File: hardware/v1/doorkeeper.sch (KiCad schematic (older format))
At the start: 29 parts, among them K1 RELAYPTH, K2 relay output, P1 ESP01 PROGRAMMING PORT, P2 ESP-01, P3 Vin, P4 ARDU PROGRAMMING PORT, P5 Software serial, P6 OLED I2C, P7 RC522, P8 Spare Pins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

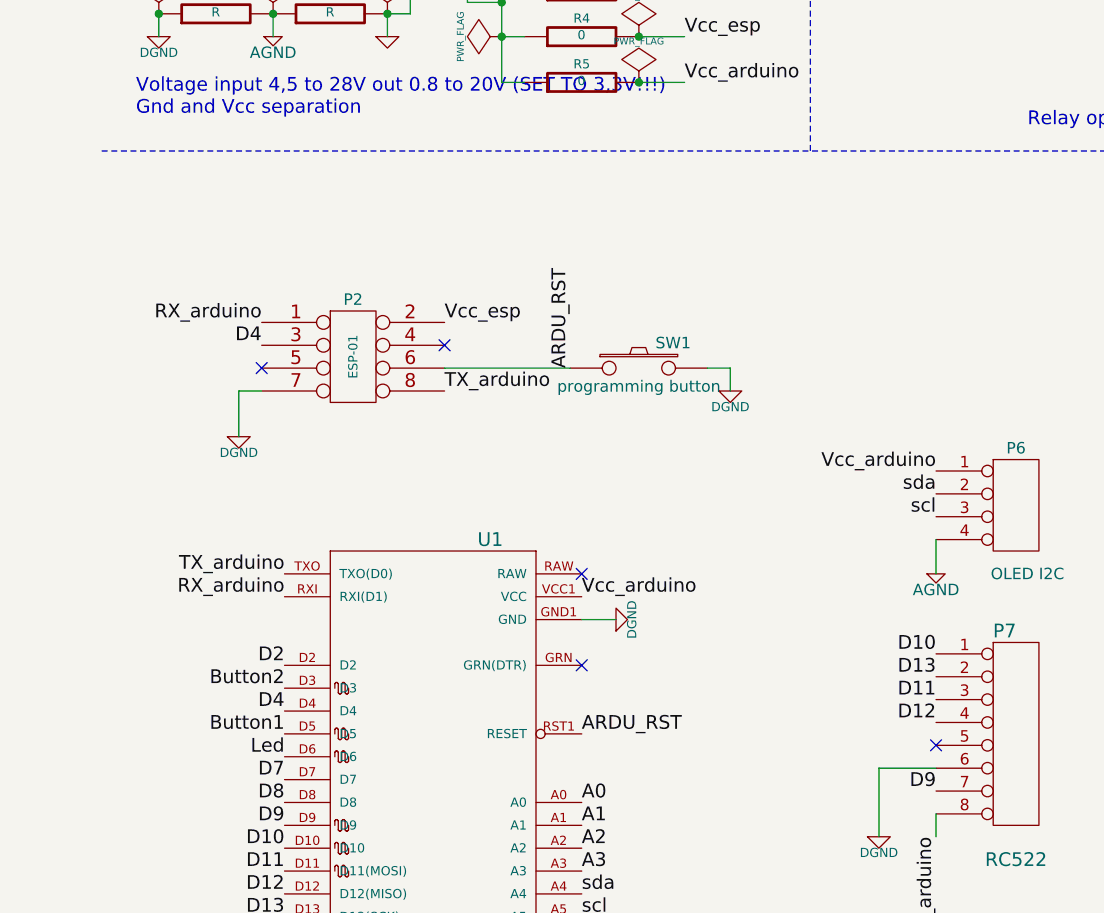
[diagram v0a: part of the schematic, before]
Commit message: corrected a schematic
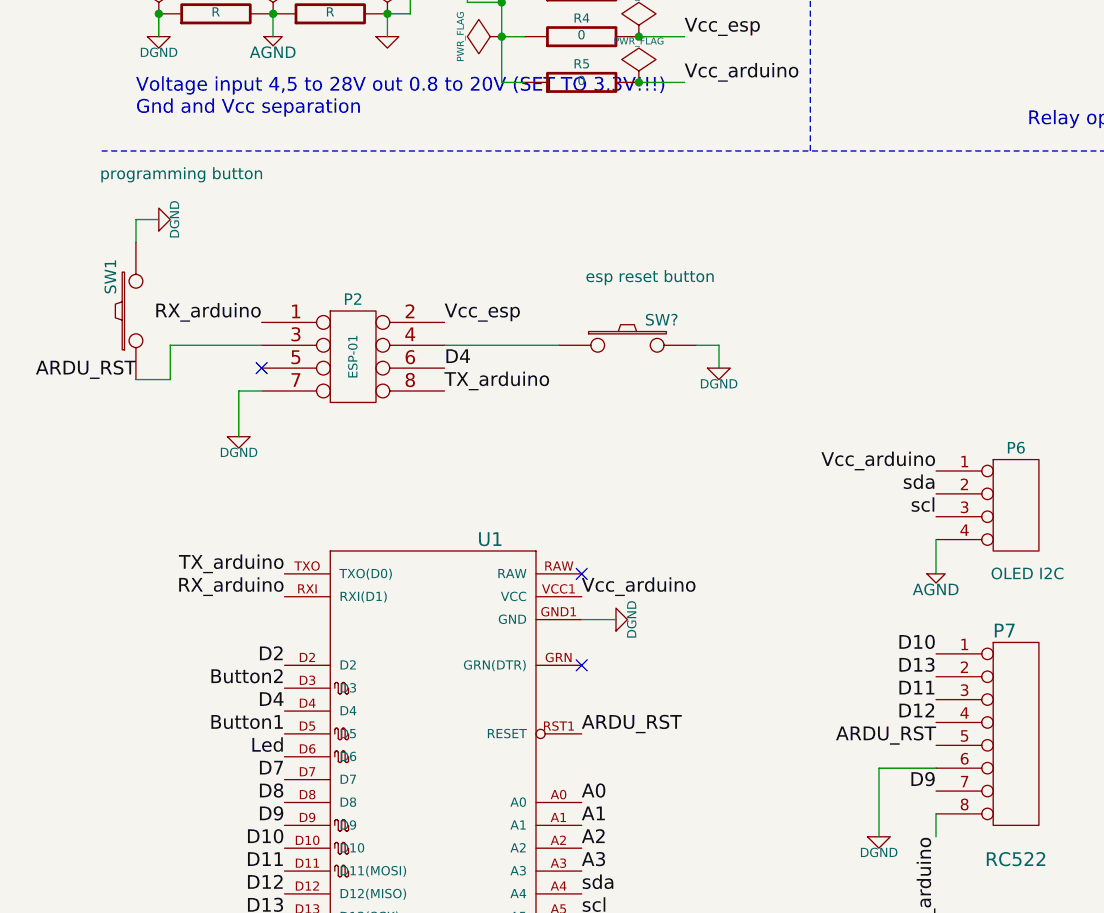
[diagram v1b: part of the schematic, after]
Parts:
- added SW?: esp reset button, ~, symbol SW_PUSH
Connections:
- net ARDU_RST: now also P2.3 (CH_PD), P7.5 (P5); no longer P2.6 (GPIO0)
- net D4: now also P2.6 (GPIO0); no longer P2.3 (CH_PD)
- net DGND: now also SW?.2
- net at P2.4 (GPIO2): now also SW?.1
- no-connect marks 6 -> 4
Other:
- moved on the sheet: SW1
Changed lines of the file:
@@
 Sheet 1 1
 Title ""
-Date "5 may 2015"
+Date "6 may 2015"
 Rev ""
 Comp ""
@@
 Text Label 1200 3650 2    60   ~ 0
 RX_arduino
-Text Label 1200 3750 2    60   ~ 0
-D4
 Text Label 1300 5350 2    60   ~ 0
 D4
@@
 Wire Wire Line
 	1100 3950 1100 4150
-NoConn ~ 2000 3750
 NoConn ~ 1200 3850
 $Comp
@@
 L SW_PUSH SW1
 U 1 1 554907CD
-P 2850 3850
-F 0 "SW1" H 3000 3960 50  0000 C CNN
-F 1 "programming button" H 2850 3770 50  0000 C CNN
-F 2 "~" H 2850 3850 60  0000 C CNN
-F 3 "~" H 2850 3850 60  0000 C CNN
-	1    2850 3850
-	1    0    0    -1
-$EndComp
-Wire Wire Line
-	3150 3850 3250 3850
-Wire Wire Line
-	3250 3850 3250 3950
+P 650 3600
+F 0 "SW1" H 800 3710 50  0000 C CNN
+F 1 "programming button" V 1250 3400 50  0000 C CNN
+F 2 "~" H 650 3600 60  0000 C CNN
+F 3 "~" H 650 3600 60  0000 C CNN
+	1    650  3600
+	0    -1   -1   0
+$EndComp
+Wire Wire Line
+	650  3300 650  3200
+Wire Wire Line
+	650  3200 750  3200
 $Comp
 L DGND #PWR012
 U 1 1 55490841
-P 3250 3950
-F 0 "#PWR012" H 3250 3950 40  0001 C CNN
-F 1 "DGND" H 3250 3880 40  0000 C CNN
-F 2 "~" H 3250 3950 60  0000 C CNN
-F 3 "~" H 3250 3950 60  0000 C CNN
-	1    3250 3950
-	1    0    0    -1
+P 750 3200
+F 0 "#PWR012" H 750 3200 40  0001 C CNN
+F 1 "DGND" H 750 3130 40  0000 C CNN
+F 2 "~" H 750 3200 60  0000 C CNN
+F 3 "~" H 750 3200 60  0000 C CNN
+	1    750  3200
+	0    -1   -1   0
 $EndComp
 $Comp
@@
 	1    0    0    -1
 $EndComp
-NoConn ~ 4150 5500
 Wire Wire Line
 	4150 5600 3900 5600
@@
 Text Label 4150 5400 2    60   ~ 0
 D12
-Wire Wire Line
-	2000 3850 2550 3850
-Text Label 2550 3850 1    60   ~ 0
+Text Label 650  3900 2    60   ~ 0
 ARDU_RST
 $Comp
@@
 Wire Wire Line
 	2850 2600 3050 2600
+Text Label 4150 5500 2    60   ~ 0
+ARDU_RST
+Wire Wire Line
+	650  3900 800  3900
+Wire Wire Line
+	800  3900 800  3750
+Wire Wire Line
+	800  3750 1200 3750
+Wire Wire Line
+	2000 3750 2500 3750
+$Comp
+L SW_PUSH SW?
+U 1 1 554A5A58
+P 2800 3750
+F 0 "SW?" H 2950 3860 50  0000 C CNN
+F 1 "esp reset button" H 2900 4050 50  0000 C CNN
+F 2 "~" H 2800 3750 60  0000 C CNN
+F 3 "~" H 2800 3750 60  0000 C CNN
+	1    2800 3750
+	1    0    0    -1
+$EndComp
+Wire Wire Line
+	3100 3750 3200 3750
+Wire Wire Line
+	3200 3750 3200 3850
+$Comp
+L DGND #PWR?
+U 1 1 554A5A60
+P 3200 3850
+F 0 "#PWR?" H 3200 3850 40  0001 C CNN
+F 1 "DGND" H 3200 3780 40  0000 C CNN
+F 2 "~" H 3200 3850 60  0000 C CNN
+F 3 "~" H 3200 3850 60  0000 C CNN
+	1    3200 3850
+	1    0    0    -1
+$EndComp
+Text Label 2000 3850 0    60   ~ 0
+D4
 $EndSCHEMATC

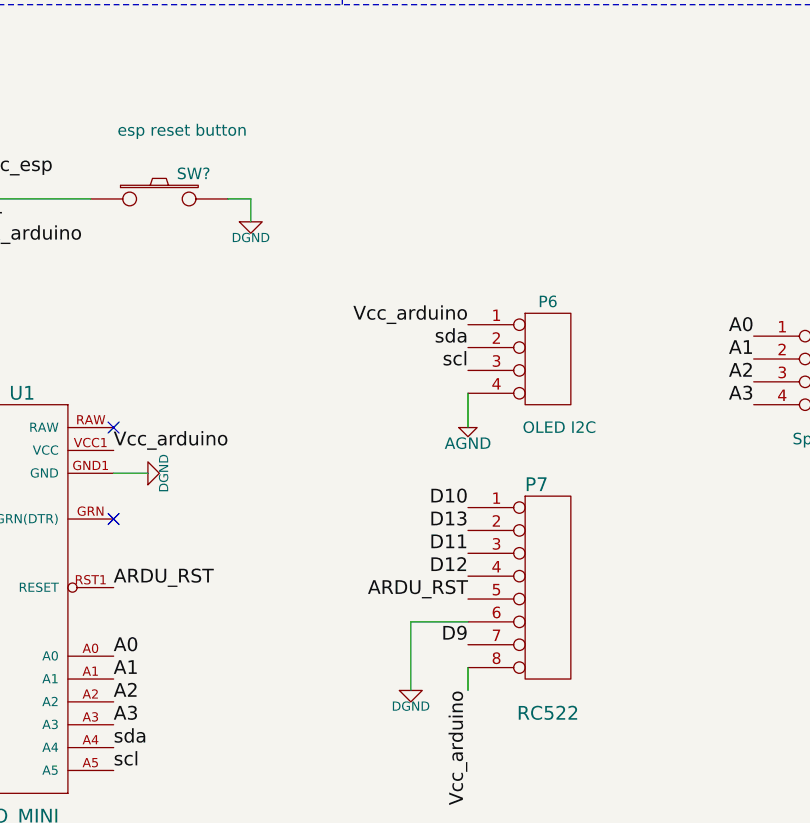
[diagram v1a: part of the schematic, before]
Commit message: corrected a schematic
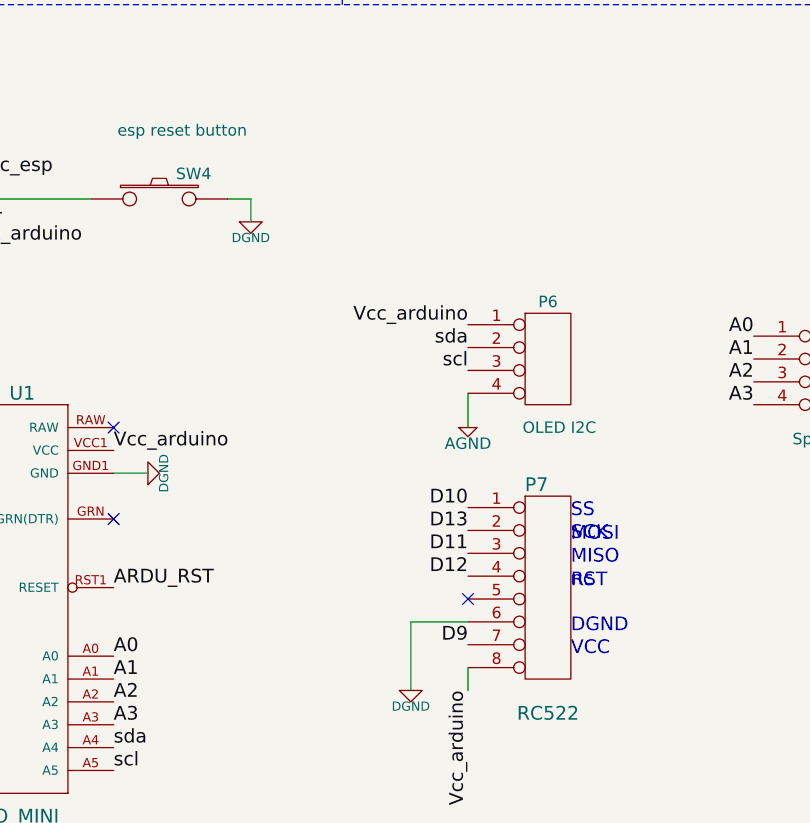
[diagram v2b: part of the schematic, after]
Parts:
- gave numbers to parts that had none: 1
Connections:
- net ARDU_RST: no longer P7.5 (P5)
- no-connect marks 4 -> 5
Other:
- note added: "DGND\n\n"
- note added: "MISO\n\n"
- note added: "MOSI\n\n"
- note added: "RST\n\n\n"
- note added: "SCK\n"
- note added: "SS"
- note added: "VCC\n\n"
- note added: "nc\n\n"
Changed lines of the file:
@@
 	750  2300 750  2400
 $Comp
-L DGND #PWR01
+L DGND #PWR1
 U 1 1 554902C3
 P 750 2400
-F 0 "#PWR01" H 750 2400 40  0001 C CNN
+F 0 "#PWR1" H 750 2400 40  0001 C CNN
 F 1 "DGND" H 750 2330 40  0000 C CNN
 F 2 "~" H 750 2400 60  0000 C CNN
@@
 $EndComp
 $Comp
-L AGND #PWR02
+L AGND #PWR5
 U 1 1 554902D2
 P 1250 2400
-F 0 "#PWR02" H 1250 2400 40  0001 C CNN
+F 0 "#PWR5" H 1250 2400 40  0001 C CNN
 F 1 "AGND" H 1250 2330 50  0000 C CNN
 F 2 "~" H 1250 2400 60  0000 C CNN
@@
 $EndComp
 $Comp
-L GND #PWR03
+L GND #PWR6
 U 1 1 554902E1
 P 1750 2400
-F 0 "#PWR03" H 1750 2400 30  0001 C CNN
+F 0 "#PWR6" H 1750 2400 30  0001 C CNN
 F 1 "GND" H 1750 2330 30  0001 C CNN
 F 2 "~" H 1750 2400 60  0000 C CNN
@@
 $EndComp
 $Comp
-L PWR_FLAG #FLG04
+L PWR_FLAG #FLG1
 U 1 1 554902FF
 P 750 2300
-F 0 "#FLG04" H 750 2395 30  0001 C CNN
+F 0 "#FLG1" H 750 2395 30  0001 C CNN
 F 1 "PWR_FLAG" H 750 2480 30  0000 C CNN
 F 2 "~" H 750 2300 60  0000 C CNN
@@
 $EndComp
 $Comp
-L PWR_FLAG #FLG05
+L PWR_FLAG #FLG2
 U 1 1 5549030C
 P 1250 2300
-F 0 "#FLG05" H 1250 2395 30  0001 C CNN
+F 0 "#FLG2" H 1250 2395 30  0001 C CNN
 F 1 "PWR_FLAG" H 1250 2480 30  0000 C CNN
 F 2 "~" H 1250 2300 60  0000 C CNN
@@
 $EndComp
 $Comp
-L PWR_FLAG #FLG06
+L PWR_FLAG #FLG3
 U 1 1 55490312
 P 1750 2300
-F 0 "#FLG06" H 1750 2395 30  0001 C CNN
+F 0 "#FLG3" H 1750 2395 30  0001 C CNN
 F 1 "PWR_FLAG" H 1750 2480 30  0000 C CNN
 F 2 "~" H 1750 2300 60  0000 C CNN
@@
 Connection ~ 2250 2250
 $Comp
-L PWR_FLAG #FLG07
+L PWR_FLAG #FLG5
 U 1 1 55490369
 P 2850 2200
-F 0 "#FLG07" H 2850 2295 30  0001 C CNN
+F 0 "#FLG5" H 2850 2295 30  0001 C CNN
 F 1 "PWR_FLAG" H 2850 2380 30  0000 C CNN
 F 2 "~" H 2850 2200 60  0000 C CNN
@@
 Connection ~ 2250 2400
 $Comp
-L PWR_FLAG #FLG08
+L PWR_FLAG #FLG6
 U 1 1 554903BB
 P 2850 2400
-F 0 "#FLG08" H 2850 2495 30  0001 C CNN
+F 0 "#FLG6" H 2850 2495 30  0001 C CNN
 F 1 "PWR_FLAG" H 2850 2580 30  0000 C CNN
 F 2 "~" H 2850 2400 60  0000 C CNN
@@
 $EndComp
 $Comp
-L PWR_FLAG #FLG09
+L PWR_FLAG #FLG7
 U 1 1 554903C1
 P 2850 2600
-F 0 "#FLG09" H 2850 2695 30  0001 C CNN
+F 0 "#FLG7" H 2850 2695 30  0001 C CNN
 F 1 "PWR_FLAG" H 2850 2780 30  0000 C CNN
 F 2 "~" H 2850 2600 60  0000 C CNN
@@
 Connection ~ 2850 2600
 $Comp
-L GND #PWR010
+L GND #PWR14
 U 1 1 554904FE
 P 4950 2350
-F 0 "#PWR010" H 4950 2350 30  0001 C CNN
+F 0 "#PWR14" H 4950 2350 30  0001 C CNN
 F 1 "GND" H 4950 2280 30  0001 C CNN
 F 2 "~" H 4950 2350 60  0000 C CNN
@@
 Vcc_relay
 $Comp
-L DGND #PWR011
+L DGND #PWR3
 U 1 1 5549054D
 P 1100 4150
-F 0 "#PWR011" H 1100 4150 40  0001 C CNN
+F 0 "#PWR3" H 1100 4150 40  0001 C CNN
 F 1 "DGND" H 1100 4080 40  0000 C CNN
 F 2 "~" H 1100 4150 60  0000 C CNN
@@
 	650  3200 750  3200
 $Comp
-L DGND #PWR012
+L DGND #PWR2
 U 1 1 55490841
 P 750 3200
-F 0 "#PWR012" H 750 3200 40  0001 C CNN
+F 0 "#PWR2" H 750 3200 40  0001 C CNN
 F 1 "DGND" H 750 3130 40  0000 C CNN
 F 2 "~" H 750 3200 60  0000 C CNN
@@
 $EndComp
 $Comp
-L DGND #PWR013
+L DGND #PWR4
 U 1 1 5549087F
 P 1100 7150
-F 0 "#PWR013" H 1100 7150 40  0001 C CNN
+F 0 "#PWR4" H 1100 7150 40  0001 C CNN
 F 1 "DGND" H 1100 7080 40  0000 C CNN
 F 2 "~" H 1100 7150 60  0000 C CNN
@@
 RX_arduino
 $Comp
-L DGND #PWR014
+L DGND #PWR7
 U 1 1 554908C1
 P 2200 7150
-F 0 "#PWR014" H 2200 7150 40  0001 C CNN
+F 0 "#PWR7" H 2200 7150 40  0001 C CNN
 F 1 "DGND" H 2200 7080 40  0000 C CNN
 F 2 "~" H 2200 7150 60  0000 C CNN
@@
 	4150 5800 4150 5900
 $Comp
-L DGND #PWR015
+L DGND #PWR12
 U 1 1 55490C81
 P 3900 5900
-F 0 "#PWR015" H 3900 5900 40  0001 C CNN
+F 0 "#PWR12" H 3900 5900 40  0001 C CNN
 F 1 "DGND" H 3900 5830 40  0000 C CNN
 F 2 "~" H 3900 5900 60  0000 C CNN
@@
 scl
 $Comp
-L AGND #PWR016
+L AGND #PWR13
 U 1 1 55490FC0
 P 4150 4750
-F 0 "#PWR016" H 4150 4750 40  0001 C CNN
+F 0 "#PWR13" H 4150 4750 40  0001 C CNN
 F 1 "AGND" H 4150 4680 50  0000 C CNN
 F 2 "~" H 4150 4750 60  0000 C CNN
@@
 NoConn ~ 2600 4750
 $Comp
-L DGND #PWR017
+L DGND #PWR8
 U 1 1 55491065
 P 2750 4950
-F 0 "#PWR017" H 2750 4950 40  0001 C CNN
+F 0 "#PWR8" H 2750 4950 40  0001 C CNN
 F 1 "DGND" H 2750 4880 40  0000 C CNN
 F 2 "~" H 2750 4950 60  0000 C CNN
@@
 	8300 2050 8300 2300
 $Comp
-L GND #PWR018
+L GND #PWR15
 U 1 1 554911B9
 P 8300 2300
-F 0 "#PWR018" H 8300 2300 30  0001 C CNN
+F 0 "#PWR15" H 8300 2300 30  0001 C CNN
 F 1 "GND" H 8300 2230 30  0001 C CNN
 F 2 "~" H 8300 2300 60  0000 C CNN
@@
 	3850 6700 3850 6750
 $Comp
-L DGND #PWR019
+L DGND #PWR10
 U 1 1 554913C9
 P 3850 6750
-F 0 "#PWR019" H 3850 6750 40  0001 C CNN
+F 0 "#PWR10" H 3850 6750 40  0001 C CNN
 F 1 "DGND" H 3850 6680 40  0000 C CNN
 F 2 "~" H 3850 6750 60  0000 C CNN
@@
 	3850 7100 3850 7150
 $Comp
-L DGND #PWR020
+L DGND #PWR11
 U 1 1 554913E5
 P 3850 7150
-F 0 "#PWR020" H 3850 7150 40  0001 C CNN
+F 0 "#PWR11" H 3850 7150 40  0001 C CNN
 F 1 "DGND" H 3850 7080 40  0000 C CNN
 F 2 "~" H 3850 7150 60  0000 C CNN
@@
 A3
 $Comp
-L PWR_FLAG #FLG021
+L PWR_FLAG #FLG4
 U 1 1 55491BE4
 P 2250 2400
-F 0 "#FLG021" H 2250 2495 30  0001 C CNN
+F 0 "#FLG4" H 2250 2495 30  0001 C CNN
 F 1 "PWR_FLAG" H 2250 2580 30  0000 C CNN
 F 2 "~" H 2250 2400 60  0000 C CNN
@@
 Wire Wire Line
 	2850 2600 3050 2600
-Text Label 4150 5500 2    60   ~ 0
-ARDU_RST
 Wire Wire Line
 	650  3900 800  3900
@@
 	2000 3750 2500 3750
 $Comp
-L SW_PUSH SW?
+L SW_PUSH SW4
 U 1 1 554A5A58
 P 2800 3750
-F 0 "SW?" H 2950 3860 50  0000 C CNN
+F 0 "SW4" H 2950 3860 50  0000 C CNN
 F 1 "esp reset button" H 2900 4050 50  0000 C CNN
 F 2 "~" H 2800 3750 60  0000 C CNN
@@
 	3200 3750 3200 3850
 $Comp
-L DGND #PWR?
+L DGND #PWR9
 U 1 1 554A5A60
 P 3200 3850
-F 0 "#PWR?" H 3200 3850 40  0001 C CNN
+F 0 "#PWR9" H 3200 3850 40  0001 C CNN
 F 1 "DGND" H 3200 3780 40  0000 C CNN
 F 2 "~" H 3200 3850 60  0000 C CNN
@@
 Text Label 2000 3850 0    60   ~ 0
 D4
+Text Notes 4600 5150 0    60   ~ 0
+SS
+Text Notes 4600 5250 0    60   ~ 0
+SCK\n
+NoConn ~ 4150 5500
+Text Notes 4600 5350 0    60   ~ 0
+MOSI\n\n
+Text Notes 4600 5450 0    60   ~ 0
+MISO\n\n
+Text Notes 4600 5550 0    60   ~ 0
+nc\n\n
+Text Notes 4600 5650 0    60   ~ 0
+RST\n\n\n
+Text Notes 4600 5850 0    60   ~ 0
+VCC\n\n
+Text Notes 4600 5750 0    60   ~ 0
+DGND\n\n
 $EndSCHEMATC

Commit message: partial routing
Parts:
- R1, R2: value R -> 0
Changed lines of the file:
@@
 Sheet 1 1
 Title ""
-Date "6 may 2015"
+Date "8 may 2015"
 Rev ""
 Comp ""
@@
 	750  2300 750  2400
 $Comp
-L DGND #PWR1
+L DGND #PWR01
 U 1 1 554902C3
 P 750 2400
-F 0 "#PWR1" H 750 2400 40  0001 C CNN
+F 0 "#PWR01" H 750 2400 40  0001 C CNN
 F 1 "DGND" H 750 2330 40  0000 C CNN
 F 2 "~" H 750 2400 60  0000 C CNN
@@
 $EndComp
 $Comp
-L AGND #PWR5
+L AGND #PWR02
 U 1 1 554902D2
 P 1250 2400
-F 0 "#PWR5" H 1250 2400 40  0001 C CNN
+F 0 "#PWR02" H 1250 2400 40  0001 C CNN
 F 1 "AGND" H 1250 2330 50  0000 C CNN
 F 2 "~" H 1250 2400 60  0000 C CNN
@@
 $EndComp
 $Comp
-L GND #PWR6
+L GND #PWR03
 U 1 1 554902E1
 P 1750 2400
-F 0 "#PWR6" H 1750 2400 30  0001 C CNN
+F 0 "#PWR03" H 1750 2400 30  0001 C CNN
 F 1 "GND" H 1750 2330 30  0001 C CNN
 F 2 "~" H 1750 2400 60  0000 C CNN
@@
 $EndComp
 $Comp
-L PWR_FLAG #FLG1
+L PWR_FLAG #FLG04
 U 1 1 554902FF
 P 750 2300
-F 0 "#FLG1" H 750 2395 30  0001 C CNN
+F 0 "#FLG04" H 750 2395 30  0001 C CNN
 F 1 "PWR_FLAG" H 750 2480 30  0000 C CNN
 F 2 "~" H 750 2300 60  0000 C CNN
@@
 $EndComp
 $Comp
-L PWR_FLAG #FLG2
+L PWR_FLAG #FLG05
 U 1 1 5549030C
 P 1250 2300
-F 0 "#FLG2" H 1250 2395 30  0001 C CNN
+F 0 "#FLG05" H 1250 2395 30  0001 C CNN
 F 1 "PWR_FLAG" H 1250 2480 30  0000 C CNN
 F 2 "~" H 1250 2300 60  0000 C CNN
@@
 $EndComp
 $Comp
-L PWR_FLAG #FLG3
+L PWR_FLAG #FLG06
 U 1 1 55490312
 P 1750 2300
-F 0 "#FLG3" H 1750 2395 30  0001 C CNN
+F 0 "#FLG06" H 1750 2395 30  0001 C CNN
 F 1 "PWR_FLAG" H 1750 2480 30  0000 C CNN
 F 2 "~" H 1750 2300 60  0000 C CNN
@@
 Connection ~ 2250 2250
 $Comp
-L PWR_FLAG #FLG5
+L PWR_FLAG #FLG07
 U 1 1 55490369
 P 2850 2200
-F 0 "#FLG5" H 2850 2295 30  0001 C CNN
+F 0 "#FLG07" H 2850 2295 30  0001 C CNN
 F 1 "PWR_FLAG" H 2850 2380 30  0000 C CNN
 F 2 "~" H 2850 2200 60  0000 C CNN
@@
 Connection ~ 2250 2400
 $Comp
-L PWR_FLAG #FLG6
+L PWR_FLAG #FLG08
 U 1 1 554903BB
 P 2850 2400
-F 0 "#FLG6" H 2850 2495 30  0001 C CNN
+F 0 "#FLG08" H 2850 2495 30  0001 C CNN
 F 1 "PWR_FLAG" H 2850 2580 30  0000 C CNN
 F 2 "~" H 2850 2400 60  0000 C CNN
@@
 $EndComp
 $Comp
-L PWR_FLAG #FLG7
+L PWR_FLAG #FLG09
 U 1 1 554903C1
 P 2850 2600
-F 0 "#FLG7" H 2850 2695 30  0001 C CNN
+F 0 "#FLG09" H 2850 2695 30  0001 C CNN
 F 1 "PWR_FLAG" H 2850 2780 30  0000 C CNN
 F 2 "~" H 2850 2600 60  0000 C CNN
@@
 Connection ~ 2850 2600
 $Comp
-L GND #PWR14
+L GND #PWR010
 U 1 1 554904FE
 P 4950 2350
-F 0 "#PWR14" H 4950 2350 30  0001 C CNN
+F 0 "#PWR010" H 4950 2350 30  0001 C CNN
 F 1 "GND" H 4950 2280 30  0001 C CNN
 F 2 "~" H 4950 2350 60  0000 C CNN
@@
 Vcc_relay
 $Comp
-L DGND #PWR3
+L DGND #PWR011
 U 1 1 5549054D
 P 1100 4150
-F 0 "#PWR3" H 1100 4150 40  0001 C CNN
+F 0 "#PWR011" H 1100 4150 40  0001 C CNN
 F 1 "DGND" H 1100 4080 40  0000 C CNN
 F 2 "~" H 1100 4150 60  0000 C CNN
@@
 	650  3200 750  3200
 $Comp
-L DGND #PWR2
+L DGND #PWR012
 U 1 1 55490841
 P 750 3200
-F 0 "#PWR2" H 750 3200 40  0001 C CNN
+F 0 "#PWR012" H 750 3200 40  0001 C CNN
 F 1 "DGND" H 750 3130 40  0000 C CNN
 F 2 "~" H 750 3200 60  0000 C CNN
@@
 $EndComp
 $Comp
-L DGND #PWR4
+L DGND #PWR013
 U 1 1 5549087F
 P 1100 7150
-F 0 "#PWR4" H 1100 7150 40  0001 C CNN
+F 0 "#PWR013" H 1100 7150 40  0001 C CNN
 F 1 "DGND" H 1100 7080 40  0000 C CNN
 F 2 "~" H 1100 7150 60  0000 C CNN
@@
 RX_arduino
 $Comp
-L DGND #PWR7
+L DGND #PWR014
 U 1 1 554908C1
 P 2200 7150
-F 0 "#PWR7" H 2200 7150 40  0001 C CNN
+F 0 "#PWR014" H 2200 7150 40  0001 C CNN
 F 1 "DGND" H 2200 7080 40  0000 C CNN
 F 2 "~" H 2200 7150 60  0000 C CNN
@@
 	4150 5800 4150 5900
 $Comp
-L DGND #PWR12
+L DGND #PWR015
 U 1 1 55490C81
 P 3900 5900
-F 0 "#PWR12" H 3900 5900 40  0001 C CNN
+F 0 "#PWR015" H 3900 5900 40  0001 C CNN
 F 1 "DGND" H 3900 5830 40  0000 C CNN
 F 2 "~" H 3900 5900 60  0000 C CNN
@@
 scl
 $Comp
-L AGND #PWR13
+L AGND #PWR016
 U 1 1 55490FC0
 P 4150 4750
-F 0 "#PWR13" H 4150 4750 40  0001 C CNN
+F 0 "#PWR016" H 4150 4750 40  0001 C CNN
 F 1 "AGND" H 4150 4680 50  0000 C CNN
 F 2 "~" H 4150 4750 60  0000 C CNN
@@
 NoConn ~ 2600 4750
 $Comp
-L DGND #PWR8
+L DGND #PWR017
 U 1 1 55491065
 P 2750 4950
-F 0 "#PWR8" H 2750 4950 40  0001 C CNN
+F 0 "#PWR017" H 2750 4950 40  0001 C CNN
 F 1 "DGND" H 2750 4880 40  0000 C CNN
 F 2 "~" H 2750 4950 60  0000 C CNN
@@
 	8300 2050 8300 2300
 $Comp
-L GND #PWR15
+L GND #PWR018
 U 1 1 554911B9
 P 8300 2300
-F 0 "#PWR15" H 8300 2300 30  0001 C CNN
+F 0 "#PWR018" H 8300 2300 30  0001 C CNN
 F 1 "GND" H 8300 2230 30  0001 C CNN
 F 2 "~" H 8300 2300 60  0000 C CNN
@@
 	3850 6700 3850 6750
 $Comp
-L DGND #PWR10
+L DGND #PWR019
 U 1 1 554913C9
 P 3850 6750
-F 0 "#PWR10" H 3850 6750 40  0001 C CNN
+F 0 "#PWR019" H 3850 6750 40  0001 C CNN
 F 1 "DGND" H 3850 6680 40  0000 C CNN
 F 2 "~" H 3850 6750 60  0000 C CNN
@@
 	3850 7100 3850 7150
 $Comp
-L DGND #PWR11
+L DGND #PWR020
 U 1 1 554913E5
 P 3850 7150
-F 0 "#PWR11" H 3850 7150 40  0001 C CNN
+F 0 "#PWR020" H 3850 7150 40  0001 C CNN
 F 1 "DGND" H 3850 7080 40  0000 C CNN
 F 2 "~" H 3850 7150 60  0000 C CNN
@@
 A3
 $Comp
-L PWR_FLAG #FLG4
+L PWR_FLAG #FLG021
 U 1 1 55491BE4
 P 2250 2400
-F 0 "#FLG4" H 2250 2495 30  0001 C CNN
+F 0 "#FLG021" H 2250 2495 30  0001 C CNN
 F 1 "PWR_FLAG" H 2250 2580 30  0000 C CNN
 F 2 "~" H 2250 2400 60  0000 C CNN
@@
 P 1000 2300
 F 0 "R1" V 1080 2300 40  0000 C CNN
-F 1 "R" V 1007 2301 40  0000 C CNN
+F 1 "0" V 1007 2301 40  0000 C CNN
 F 2 "~" V 930 2300 30  0000 C CNN
 F 3 "~" H 1000 2300 30  0000 C CNN
@@
 P 1500 2300
 F 0 "R2" V 1580 2300 40  0000 C CNN
-F 1 "R" V 1507 2301 40  0000 C CNN
+F 1 "0" V 1507 2301 40  0000 C CNN
 F 2 "~" V 1430 2300 30  0000 C CNN
 F 3 "~" H 1500 2300 30  0000 C CNN
@@
 	3200 3750 3200 3850
 $Comp
-L DGND #PWR9
+L DGND #PWR022
 U 1 1 554A5A60
 P 3200 3850
-F 0 "#PWR9" H 3200 3850 40  0001 C CNN
+F 0 "#PWR022" H 3200 3850 40  0001 C CNN
 F 1 "DGND" H 3200 3780 40  0000 C CNN
 F 2 "~" H 3200 3850 60  0000 C CNN
